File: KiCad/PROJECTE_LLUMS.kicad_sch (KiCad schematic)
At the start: 0 parts

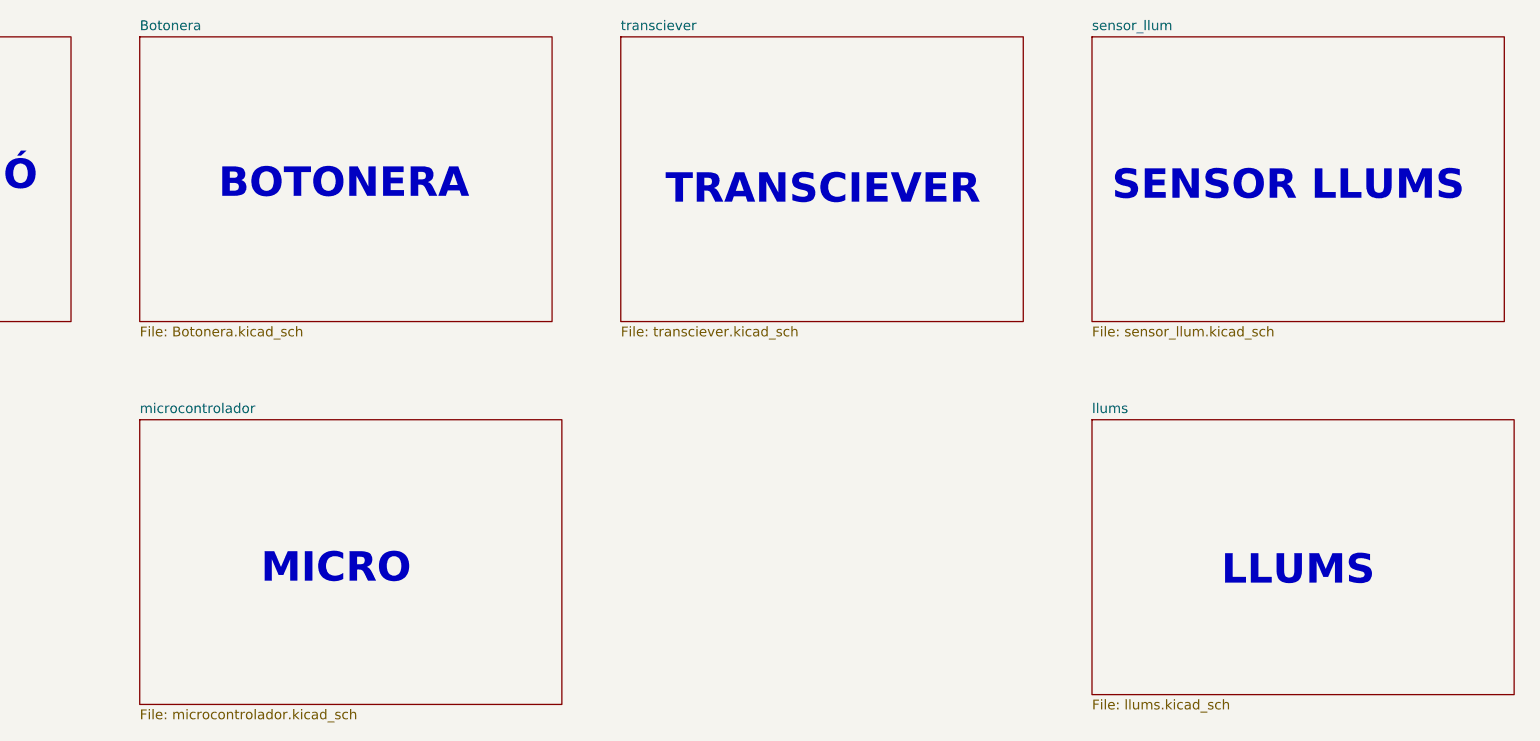
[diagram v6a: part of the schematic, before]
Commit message: he esborrat els esquemàtics del transciever i USART
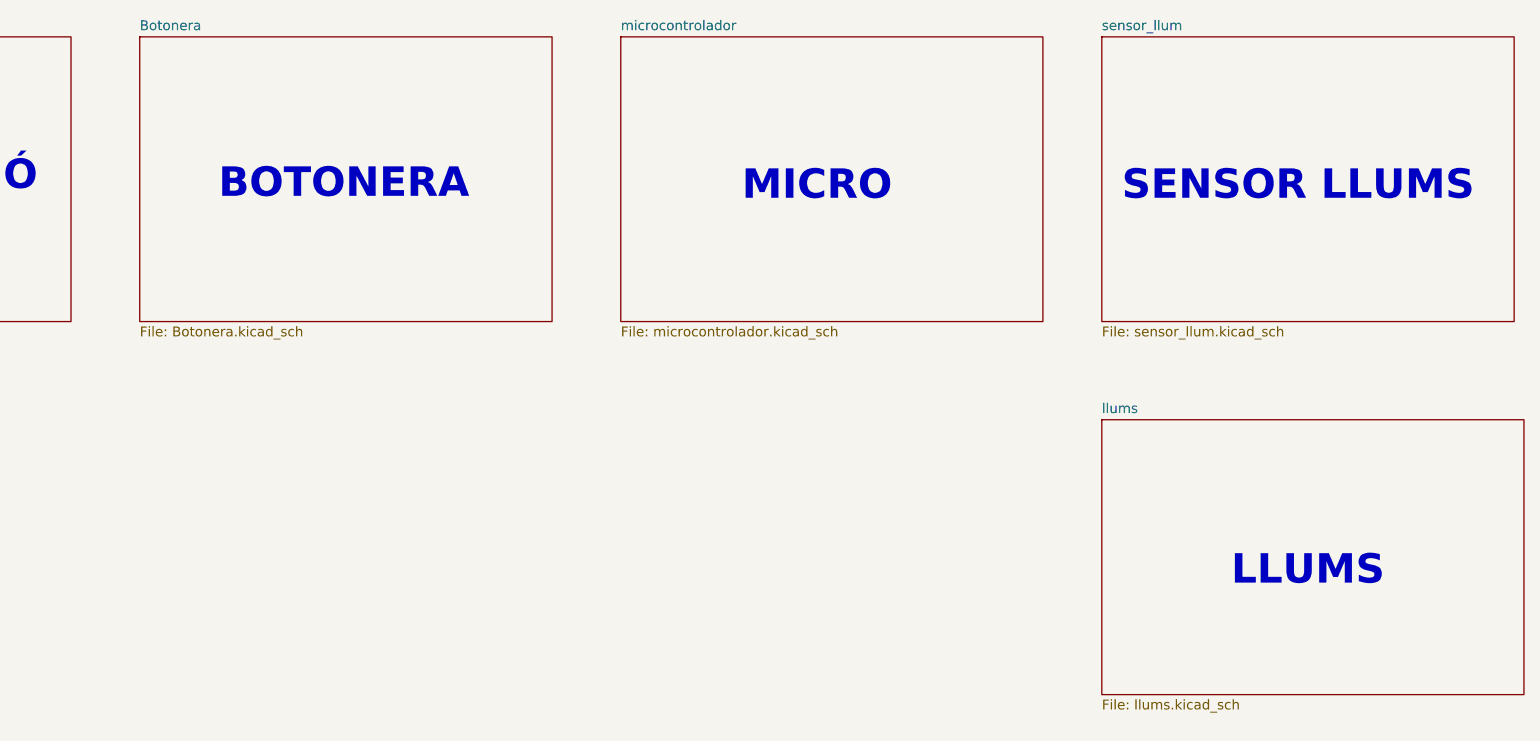
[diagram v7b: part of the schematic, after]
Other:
- removed sheet transciever
- note removed: "TRANSCIEVER"
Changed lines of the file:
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@@
 	(text "MICRO"
 		(exclude_from_sim no)
-		(at 113.03 95.504 0)
+		(at 175.26 45.974 0)
 		(effects
 			(font
@@
 	(text "LLUMS\n"
 		(exclude_from_sim no)
-		(at 237.49 95.758 0)
-		(effects
-			(font
-				(size 3.81 3.81)
-				(thickness 0.762)
-				(bold yes)
-			)
-		)
-	)
-	(text "TRANSCIEVER\n"
-		(exclude_from_sim no)
-		(at 176.022 46.482 0)
+		(at 238.76 95.758 0)
 		(effects
 			(font
@@
 	(text "SENSOR LLUMS\n"
 		(exclude_from_sim no)
-		(at 236.22 45.974 0)
-		(effects
-			(font
-				(size 3.81 3.81)
-				(thickness 0.762)
-				(bold yes)
-			)
-		)
-	)
-	(sheet
-		(at 210.82 76.2)
+		(at 237.49 45.974 0)
+		(effects
+			(font
+				(size 3.81 3.81)
+				(thickness 0.762)
+				(bold yes)
+			)
+		)
+	)
+	(sheet
+		(at 212.09 76.2)
 		(size 54.61 35.56)
 		(exclude_from_sim no)
@@
 		)
 		(property "Sheetname" "llums"
-			(at 210.82 75.4884 0)
+			(at 212.09 75.4884 0)
 			(effects
 				(font
@@
 		)
 		(property "Sheetfile" "llums.kicad_sch"
-			(at 210.82 112.3446 0)
+			(at 212.09 112.3446 0)
 			(effects
 				(font
@@
 	)
 	(sheet
-		(at 210.82 26.67)
+		(at 212.09 26.67)
 		(size 53.34 36.83)
 		(exclude_from_sim no)
@@
 		)
 		(property "Sheetname" "sensor_llum"
-			(at 210.82 25.9584 0)
+			(at 212.09 25.9584 0)
 			(effects
 				(font
@@
 		)
 		(property "Sheetfile" "sensor_llum.kicad_sch"
-			(at 210.82 64.0846 0)
+			(at 212.09 64.0846 0)
 			(effects
 				(font
@@
 	)
 	(sheet
-		(at 87.63 76.2)
+		(at 149.86 26.67)
 		(size 54.61 36.83)
 		(exclude_from_sim no)
@@
 		)
 		(property "Sheetname" "microcontrolador"
-			(at 87.63 75.4884 0)
+			(at 149.86 25.9584 0)
 			(effects
 				(font
@@
 		)
 		(property "Sheetfile" "microcontrolador.kicad_sch"
-			(at 87.63 113.6146 0)
+			(at 149.86 64.0846 0)
 			(effects
 				(font
@@
 				)
 			)
-		)
-	)
-	(sheet
-		(at 149.86 26.67)
-		(size 52.07 36.83)
-		(exclude_from_sim no)
-		(in_bom yes)
-		(on_board yes)
-		(dnp no)
-		(fields_autoplaced yes)
-		(stroke
-			(width 0.1524)
-			(type solid)
-		)
-		(fill
-			(color 0 0 0 0.0000)
-		)
-		(property "Sheetname" "transciever"
-			(at 149.86 25.9584 0)
-			(effects
-				(font
-					(size 1.27 1.27)
-				)
-				(justify left bottom)
-			)
-		)
-		(property "Sheetfile" "transciever.kicad_sch"
-			(at 149.86 64.0846 0)
-			(effects
-				(font
-					(size 1.27 1.27)
-				)
-				(justify left top)
-			)
-		)
-		(instances
-			(project "PROJECTE_LLUMS"
-				(path "/b4874c87-978f-427f-bc45-3635f8629977"
-					(page "5")
-				)
-			)
